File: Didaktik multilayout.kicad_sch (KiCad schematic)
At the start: 122 parts, among them J1 Conn_01x04_MountingPin, J2 AVR-ISP-6, J3 Conn_01x03, SW1 SW_Push_45deg, SW10 SW_Push_45deg, SW11 SW_Push_45deg, SW12 SW_Push_45deg, SW13 SW_Push_45deg, SW14 SW_Push_45deg, SW15 SW_Push_45deg, SW16 SW_Push_45deg, SW17 SW_Push_45deg, SW18 SW_Push_45deg, SW19 SW_Push_45deg, SW2 SW_Push_45deg, SW20 SW_Push_45deg, SW21 SW_Push_45deg, SW22 SW_Push_45deg, SW23 SW_Push_45deg, SW24 SW_Push_45deg, SW25 SW_Push_45deg, SW26 SW_Push_45deg, SW27 SW_Push_45deg, SW28 SW_Push_45deg, SW29 SW_Push_45deg, SW3 SW_Push_45deg, SW30 SW_Push_45deg, SW31 SW_Push_45deg, SW31a1 SW_Push_45deg, SW32 SW_Push_45deg, SW32a1 SW_Push_45deg, SW33 SW_Push_45deg, SW33a1 SW_Push_45deg, SW34 SW_Push_45deg, SW34a1 SW_Push_45deg, SW34b1 SW_Push_45deg, SW35 SW_Push_45deg, SW35a1 SW_Push_45deg, SW35b1 SW_Push_45deg, SW35c1 SW_Push_45deg, SW36 SW_Push_45deg, SW36a1 SW_Push_45deg, SW36b1 SW_Push_45deg, SW36c1 SW_Push_45deg, SW37 SW_Push_45deg, SW37a1 SW_Push_45deg, SW37b1 SW_Push_45deg, SW38 SW_Push_45deg, SW38a1 SW_Push_45deg, SW39 SW_Push_45deg, SW39a1 SW_Push_45deg, SW4 SW_Push_45deg, SW40 SW_Push_45deg, SW40a1 SW_Push_45deg, SW41 RotaryEncoder_Switch, SW42 RotaryEncoder_Switch, SW5 SW_Push_45deg, SW6 SW_Push_45deg, SW7 SW_Push_45deg, SW8 SW_Push_45deg, SW9 SW_Push_45deg, U1 ATmega32U4-M, Y1 Crystal_GND24_Small

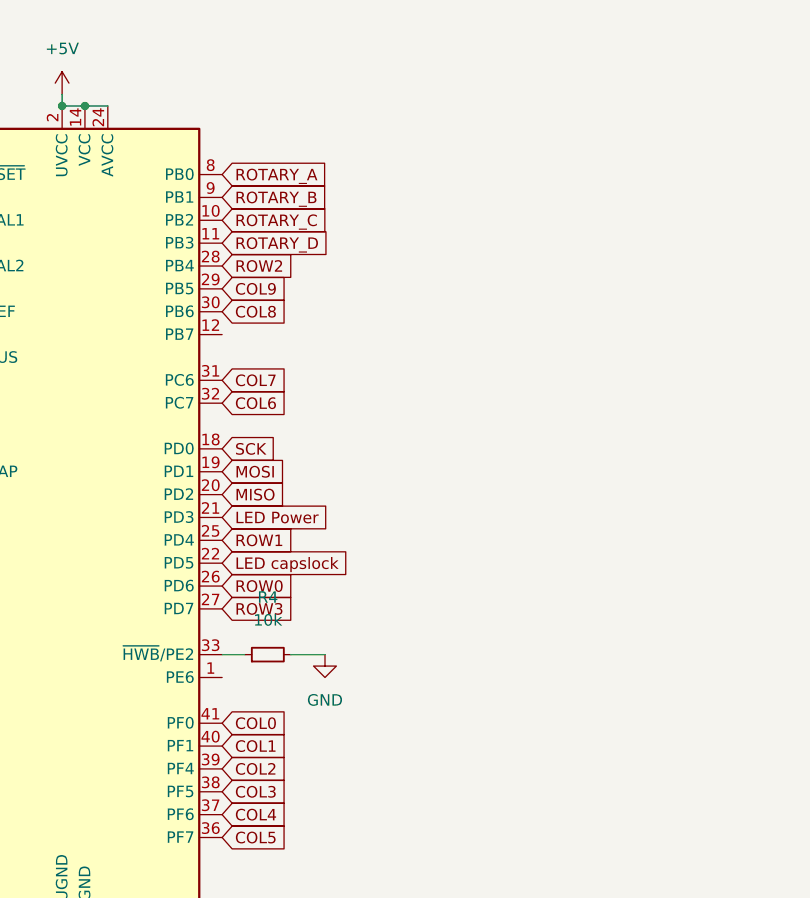
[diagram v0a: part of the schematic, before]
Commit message: added buzzer
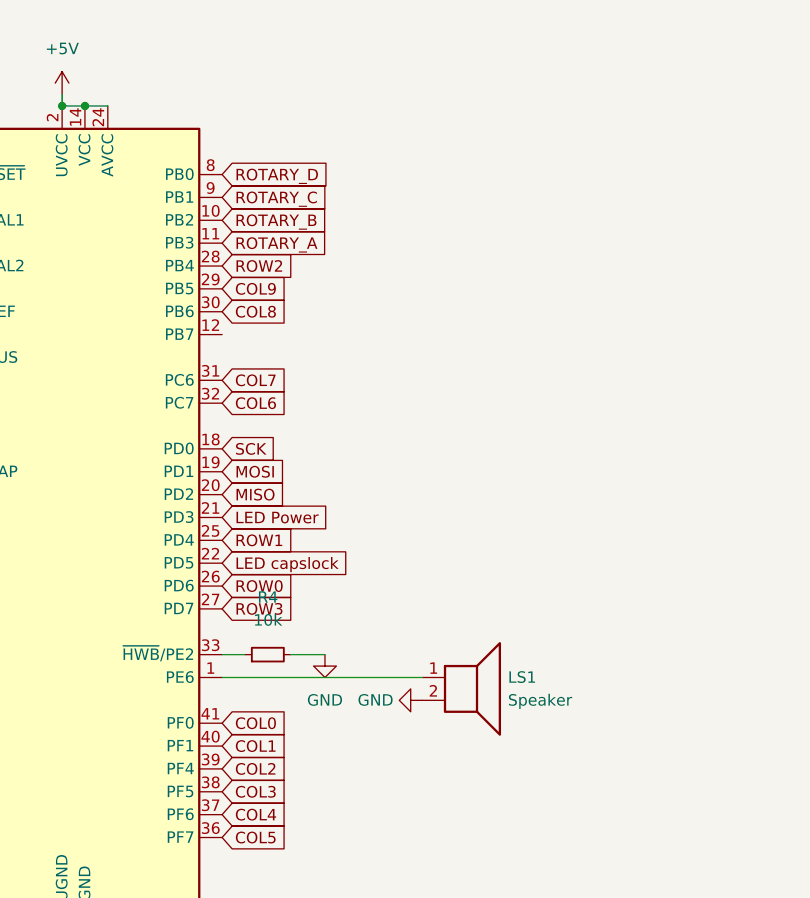
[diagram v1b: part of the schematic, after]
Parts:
- added LS1: Speaker, Keebio-Parts:AST1109MLTRQ, symbol Device:Speaker
- J3: footprint Connector_PinHeader_2.54mm:PinHeader_1x03_P2.54mm_Vertical -> Connector_PinSocket_2.00mm:PinSocket_1x03_P2.00mm_Vertical
- SW41, SW42: footprint Keebio-Parts:RotaryEncoder_Alps_EC11E-Switch_Vertical_H20mm -> Keebio-Parts:RotaryEncoder_EC11-no-legs
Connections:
- net GND: now also LS1.2
- net ROTARY_A: now also U1.11 (PB3); no longer U1.8 (PB0)
- net ROTARY_B: now also U1.10 (PB2); no longer U1.9 (PB1)
- net ROTARY_C: now also U1.9 (PB1); no longer U1.10 (PB2)
- net ROTARY_D: now also U1.8 (PB0); no longer U1.11 (PB3)
- net at U1.1 (PE6): now also LS1.1
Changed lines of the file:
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@@
     (stroke (width 0) (type default) (color 0 0 0 0))
   )
+  (wire (pts (xy 68.58 87.63) (xy 90.805 87.63))
+    (stroke (width 0) (type default) (color 0 0 0 0))
+  )
   (wire (pts (xy 196.215 88.265) (xy 196.215 107.95))
     (stroke (width 0) (type default) (color 0 0 0 0))
@@
     )
   )
-  (global_label "ROTARY_A" (shape input) (at 68.58 31.75 0) (fields_autoplaced)
+  (global_label "ROTARY_A" (shape input) (at 68.58 39.37 0) (fields_autoplaced)
     (effects (font (size 1.27 1.27)) (justify left))
-    (property "Intersheet References" "${INTERSHEET_REFS}" (id 0) (at 80.0645 31.8294 0)
+    (property "Intersheet References" "${INTERSHEET_REFS}" (id 0) (at 80.0645 39.4494 0)
       (effects (font (size 1.27 1.27)) (justify left) hide)
     )
@@
     )
   )
-  (global_label "ROTARY_B" (shape input) (at 68.58 34.29 0) (fields_autoplaced)
+  (global_label "ROTARY_B" (shape input) (at 68.58 36.83 0) (fields_autoplaced)
     (effects (font (size 1.27 1.27)) (justify left))
-    (property "Intersheet References" "${INTERSHEET_REFS}" (id 0) (at 80.246 34.3694 0)
+    (property "Intersheet References" "${INTERSHEET_REFS}" (id 0) (at 80.246 36.9094 0)
       (effects (font (size 1.27 1.27)) (justify left) hide)
     )
@@
     )
   )
-  (global_label "ROTARY_C" (shape input) (at 68.58 36.83 0) (fields_autoplaced)
+  (global_label "ROTARY_C" (shape input) (at 68.58 34.29 0) (fields_autoplaced)
     (effects (font (size 1.27 1.27)) (justify left))
-    (property "Intersheet References" "${INTERSHEET_REFS}" (id 0) (at 80.246 36.7506 0)
+    (property "Intersheet References" "${INTERSHEET_REFS}" (id 0) (at 80.246 34.2106 0)
       (effects (font (size 1.27 1.27)) (justify left) hide)
     )
@@
     )
   )
-  (global_label "ROTARY_D" (shape input) (at 68.58 39.37 0) (fields_autoplaced)
+  (global_label "ROTARY_D" (shape input) (at 68.58 31.75 0) (fields_autoplaced)
     (effects (font (size 1.27 1.27)) (justify left))
-    (property "Intersheet References" "${INTERSHEET_REFS}" (id 0) (at 80.246 39.2906 0)
+    (property "Intersheet References" "${INTERSHEET_REFS}" (id 0) (at 80.246 31.6706 0)
       (effects (font (size 1.27 1.27)) (justify left) hide)
     )
@@
     (pin "2")
   )
+  (symbol (lib_id "power:GND") (at 90.805 90.17 270) (unit 1)
+    (in_bom yes) (on_board yes) (fields_autoplaced)
+    (property "Reference" "#PWR0125" (id 0) (at 84.455 90.17 0)
+      (effects (font (size 1.27 1.27)) hide)
+    )
+    (property "Value" "GND" (id 1) (at 87.63 90.1699 90)
+      (effects (font (size 1.27 1.27)) (justify right))
+    )
+    (property "Footprint" "" (id 2) (at 90.805 90.17 0)
+      (effects (font (size 1.27 1.27)) hide)
+    )
+    (property "Datasheet" "" (id 3) (at 90.805 90.17 0)
+      (effects (font (size 1.27 1.27)) hide)
+    )
+    (pin "1")
+  )
   (symbol (lib_id "power:GND") (at 48.26 115.57 0) (unit 1)
     (in_bom yes) (on_board yes) (fields_autoplaced)
@@
     (property "Reference" "J3" (id 0) (at 131.445 120.015 0))
     (property "Value" "Conn_01x03" (id 1) (at 131.445 130.175 0))
-    (property "Footprint" "Connector_PinHeader_2.54mm:PinHeader_1x03_P2.54mm_Vertical" (id 2) (at 131.445 125.095 0)
+    (property "Footprint" "Connector_PinSocket_2.00mm:PinSocket_1x03_P2.00mm_Vertical" (id 2) (at 131.445 125.095 0)
       (effects (font (size 1.27 1.27)) hide)
     )
@@
     (property "Reference" "SW42" (id 0) (at 239.395 82.55 0))
     (property "Value" "RotaryEncoder_Switch" (id 1) (at 239.395 80.01 0))
-    (property "Footprint" "Keebio-Parts:RotaryEncoder_Alps_EC11E-Switch_Vertical_H20mm" (id 2) (at 243.205 76.454 0)
+    (property "Footprint" "Keebio-Parts:RotaryEncoder_EC11-no-legs" (id 2) (at 243.205 76.454 0)
       (effects (font (size 1.27 1.27)) hide)
     )
@@
     (property "Reference" "SW41" (id 0) (at 153.67 28.575 0))
     (property "Value" "RotaryEncoder_Switch" (id 1) (at 153.67 31.115 0))
-    (property "Footprint" "Keebio-Parts:RotaryEncoder_Alps_EC11E-Switch_Vertical_H20mm" (id 2) (at 149.86 34.671 0)
+    (property "Footprint" "Keebio-Parts:RotaryEncoder_EC11-no-legs" (id 2) (at 149.86 34.671 0)
       (effects (font (size 1.27 1.27)) hide)
     )
@@
     (pin "2")
   )
+  (symbol (lib_id "Device:Speaker") (at 95.885 87.63 0) (unit 1)
+    (in_bom yes) (on_board yes) (fields_autoplaced)
+    (property "Reference" "LS1" (id 0) (at 100.33 87.6299 0)
+      (effects (font (size 1.27 1.27)) (justify left))
+    )
+    (property "Value" "Speaker" (id 1) (at 100.33 90.1699 0)
+      (effects (font (size 1.27 1.27)) (justify left))
+    )
+    (property "Footprint" "Keebio-Parts:AST1109MLTRQ" (id 2) (at 95.885 92.71 0)
+      (effects (font (size 1.27 1.27)) hide)
+    )
+    (property "Datasheet" "~" (id 3) (at 95.631 88.9 0)
+      (effects (font (size 1.27 1.27)) hide)
+    )
+    (pin "1")
+    (pin "2")
+  )
   (symbol (lib_id "Switch:SW_Push_45deg") (at 199.39 105.41 0) (mirror y) (unit 1)
     (in_bom yes) (on_board yes)
@@
       (reference "#PWR0124") (unit 1) (value "GND") (footprint "")
     )
+    (path "/46e8824a-8f30-44a6-8611-6e7599dbffe8"
+      (reference "#PWR0125") (unit 1) (value "GND") (footprint "")
+    )
     (path "/4288a19a-13d9-4091-890e-2cc91277147e"
       (reference "C1") (unit 1) (value "0.1uF") (footprint "Capacitor_SMD:C_0402_1005Metric")
@@
     )
     (path "/909e0f83-af71-499c-861a-44ecae1cdab9"
-      (reference "J3") (unit 1) (value "Conn_01x03") (footprint "Connector_PinHeader_2.54mm:PinHeader_1x03_P2.54mm_Vertical")
+      (reference "J3") (unit 1) (value "Conn_01x03") (footprint "Connector_PinSocket_2.00mm:PinSocket_1x03_P2.00mm_Vertical")
+    )
+    (path "/fbecd2a9-a948-4ba1-8e78-655fa59a6c74"
+      (reference "LS1") (unit 1) (value "Speaker") (footprint "Keebio-Parts:AST1109MLTRQ")
     )
     (path "/1b233532-9656-4e4e-a0b7-8260db2f2d5f"
@@
     )
     (path "/b5d6c90d-09f6-4204-96c6-5159b8bf8ade"
-      (reference "SW41") (unit 1) (value "RotaryEncoder_Switch") (footprint "Keebio-Parts:RotaryEncoder_Alps_EC11E-Switch_Vertical_H20mm")
+      (reference "SW41") (unit 1) (value "RotaryEncoder_Switch") (footprint "Keebio-Parts:RotaryEncoder_EC11-no-legs")
     )
     (path "/b188310f-7fb9-45a6-a509-13d28fe15160"
-      (reference "SW42") (unit 1) (value "RotaryEncoder_Switch") (footprint "Keebio-Parts:RotaryEncoder_Alps_EC11E-Switch_Vertical_H20mm")
+      (reference "SW42") (unit 1) (value "RotaryEncoder_Switch") (footprint "Keebio-Parts:RotaryEncoder_EC11-no-legs")
     )
     (path "/24a36d74-2c9b-468a-8a3d-4eb2fe2b6c67"

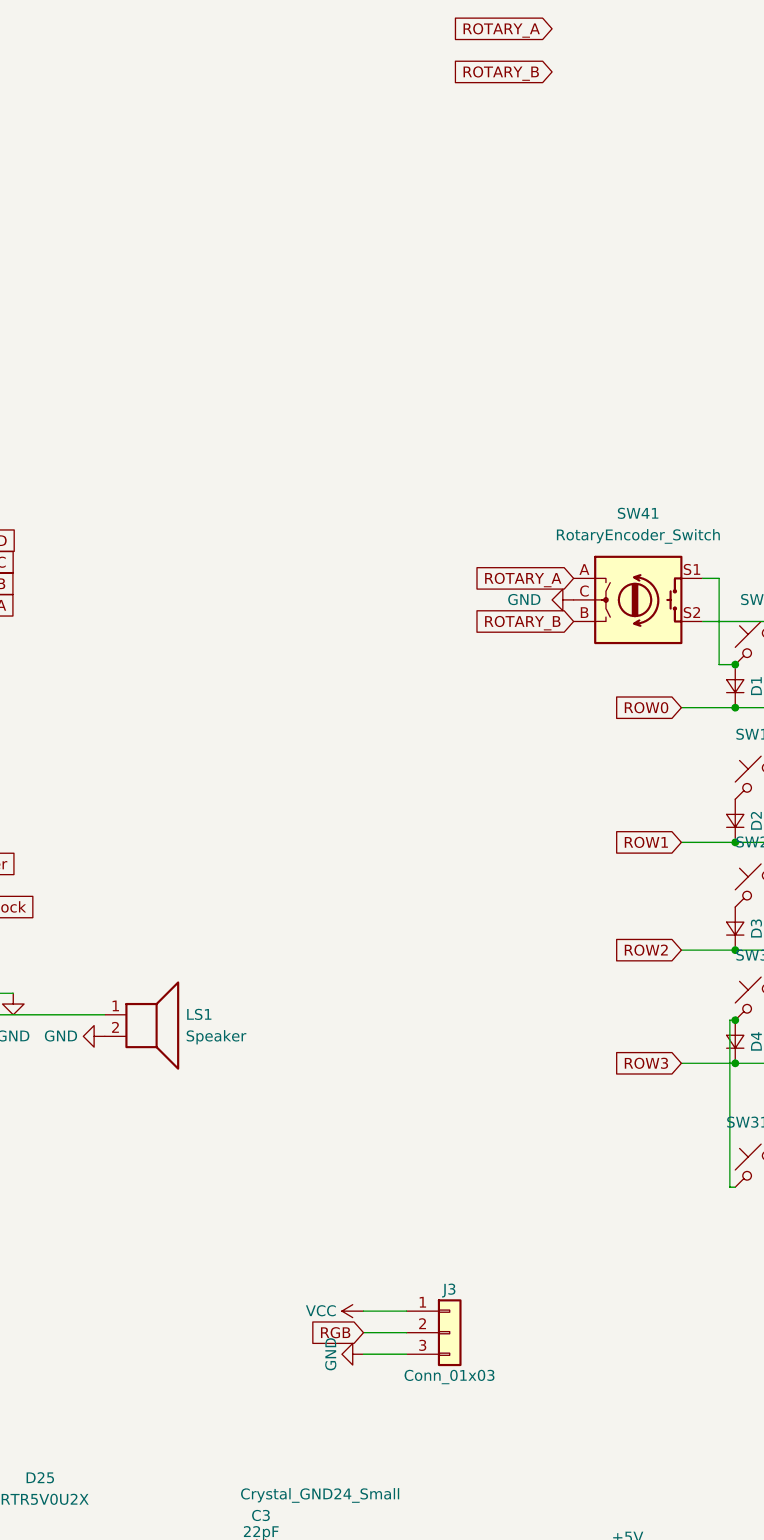
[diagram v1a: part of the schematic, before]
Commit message: created production files, pdfs for review
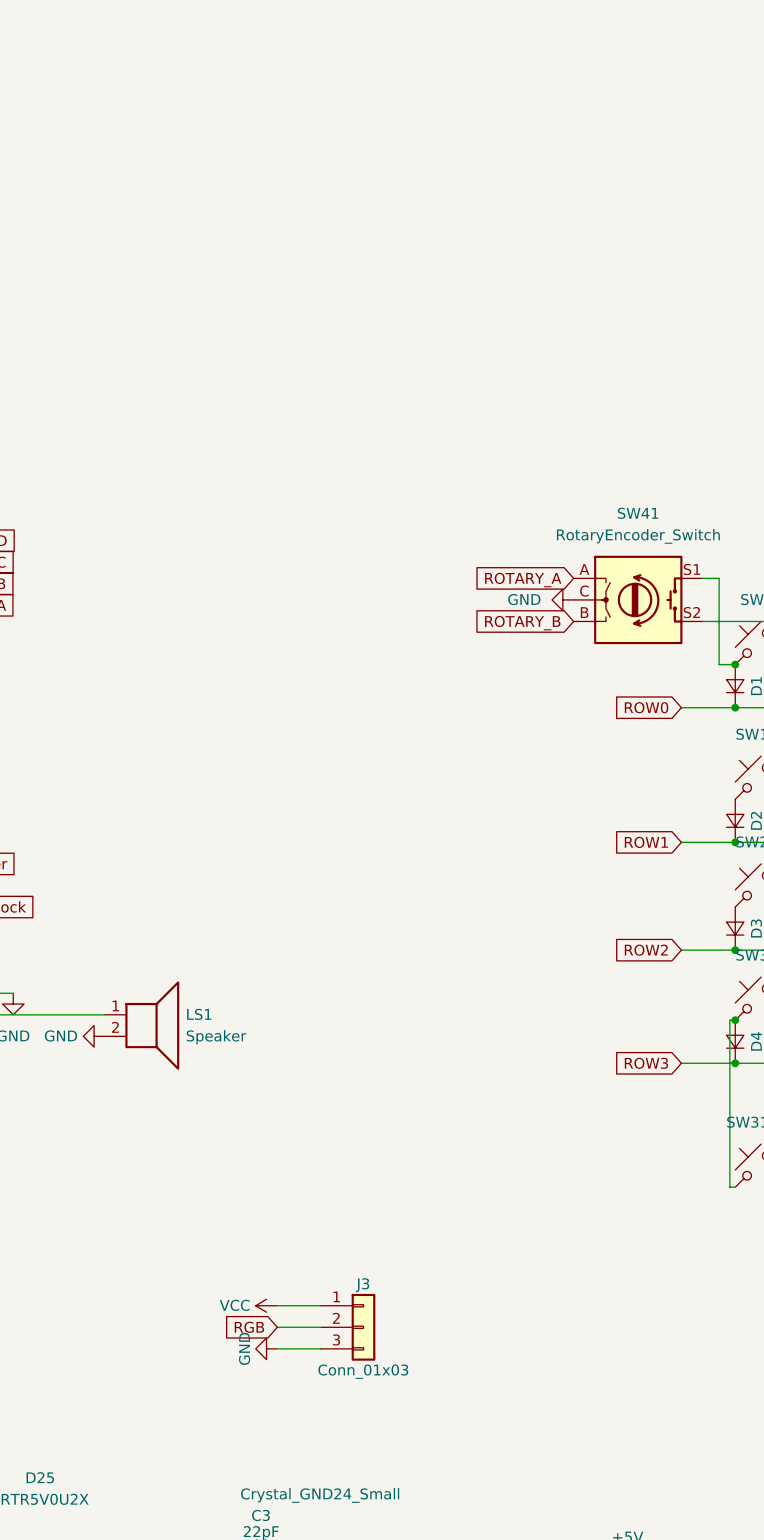
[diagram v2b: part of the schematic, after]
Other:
- moved on the sheet: J3
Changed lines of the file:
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@@
     (stroke (width 0) (type default) (color 0 0 0 0))
   )
-  (wire (pts (xy 121.285 122.555) (xy 126.365 122.555))
+  (wire (pts (xy 111.125 121.92) (xy 116.205 121.92))
     (stroke (width 0) (type default) (color 0 0 0 0))
   )
@@
     (stroke (width 0) (type default) (color 0 0 0 0))
   )
-  (wire (pts (xy 121.285 127.635) (xy 126.365 127.635))
+  (wire (pts (xy 111.125 127) (xy 116.205 127))
     (stroke (width 0) (type default) (color 0 0 0 0))
   )
@@
     (stroke (width 0) (type default) (color 0 0 0 0))
   )
-  (wire (pts (xy 121.285 125.095) (xy 126.365 125.095))
+  (wire (pts (xy 111.125 124.46) (xy 116.205 124.46))
     (stroke (width 0) (type default) (color 0 0 0 0))
   )
@@
     )
   )
-  (global_label "ROTARY_B" (shape input) (at 143.51 -23.495 180) (fields_autoplaced)
-    (effects (font (size 1.27 1.27)) (justify right))
-    (property "Intersheet References" "${INTERSHEET_REFS}" (id 0) (at 131.844 -23.5744 0)
-      (effects (font (size 1.27 1.27)) (justify right) hide)
-    )
-  )
   (global_label "ROTARY_A" (shape input) (at 146.05 36.195 180) (fields_autoplaced)
     (effects (font (size 1.27 1.27)) (justify right))
@@
     )
   )
-  (global_label "ROTARY_A" (shape input) (at 143.51 -28.575 180) (fields_autoplaced)
-    (effects (font (size 1.27 1.27)) (justify right))
-    (property "Intersheet References" "${INTERSHEET_REFS}" (id 0) (at 132.0255 -28.6544 0)
-      (effects (font (size 1.27 1.27)) (justify right) hide)
-    )
-  )
   (global_label "COL9" (shape input) (at 68.58 44.45 0) (fields_autoplaced)
     (effects (font (size 1.27 1.27)) (justify left))
@@
     )
   )
-  (global_label "RGB" (shape input) (at 121.285 125.095 180) (fields_autoplaced)
+  (global_label "RGB" (shape input) (at 111.125 124.46 180) (fields_autoplaced)
     (effects (font (size 1.27 1.27)) (justify right))
-    (property "Intersheet References" "${INTERSHEET_REFS}" (id 0) (at -40.005 77.47 0)
+    (property "Intersheet References" "${INTERSHEET_REFS}" (id 0) (at -50.165 76.835 0)
       (effects (font (size 1.27 1.27)) hide)
     )
@@
     (pin "2")
   )
-  (symbol (lib_id "power:VCC") (at 121.285 122.555 90) (unit 1)
-    (in_bom yes) (on_board yes) (fields_autoplaced)
-    (property "Reference" "#PWR0115" (id 0) (at 125.095 122.555 0)
-      (effects (font (size 1.27 1.27)) hide)
-    )
-    (property "Value" "VCC" (id 1) (at 118.11 122.5549 90)
+  (symbol (lib_id "power:VCC") (at 111.125 121.92 90) (unit 1)
+    (in_bom yes) (on_board yes) (fields_autoplaced)
+    (property "Reference" "#PWR0115" (id 0) (at 114.935 121.92 0)
+      (effects (font (size 1.27 1.27)) hide)
+    )
+    (property "Value" "VCC" (id 1) (at 107.95 121.9199 90)
       (effects (font (size 1.27 1.27)) (justify left))
     )
-    (property "Footprint" "" (id 2) (at 121.285 122.555 0)
-      (effects (font (size 1.27 1.27)) hide)
-    )
-    (property "Datasheet" "" (id 3) (at 121.285 122.555 0)
+    (property "Footprint" "" (id 2) (at 111.125 121.92 0)
+      (effects (font (size 1.27 1.27)) hide)
+    )
+    (property "Datasheet" "" (id 3) (at 111.125 121.92 0)
       (effects (font (size 1.27 1.27)) hide)
     )
@@
     (pin "2")
   )
-  (symbol (lib_id "alpha_pro_micro-rescue:Conn_01x03") (at 131.445 125.095 0) (unit 1)
-    (in_bom yes) (on_board yes)
-    (property "Reference" "J3" (id 0) (at 131.445 120.015 0))
-    (property "Value" "Conn_01x03" (id 1) (at 131.445 130.175 0))
-    (property "Footprint" "Connector_PinSocket_2.00mm:PinSocket_1x03_P2.00mm_Vertical" (id 2) (at 131.445 125.095 0)
-      (effects (font (size 1.27 1.27)) hide)
-    )
-    (property "Datasheet" "" (id 3) (at 131.445 125.095 0)
+  (symbol (lib_id "alpha_pro_micro-rescue:Conn_01x03") (at 121.285 124.46 0) (unit 1)
+    (in_bom yes) (on_board yes)
+    (property "Reference" "J3" (id 0) (at 121.285 119.38 0))
+    (property "Value" "Conn_01x03" (id 1) (at 121.285 129.54 0))
+    (property "Footprint" "Connector_PinSocket_2.00mm:PinSocket_1x03_P2.00mm_Vertical" (id 2) (at 121.285 124.46 0)
+      (effects (font (size 1.27 1.27)) hide)
+    )
+    (property "Datasheet" "" (id 3) (at 121.285 124.46 0)
       (effects (font (size 1.27 1.27)) hide)
     )
@@
     (pin "1")
   )
-  (symbol (lib_id "power:GND") (at 121.285 127.635 270) (unit 1)
-    (in_bom yes) (on_board yes)
-    (property "Reference" "#PWR0120" (id 0) (at 114.935 127.635 0)
-      (effects (font (size 1.27 1.27)) hide)
-    )
-    (property "Value" "GND" (id 1) (at 117.475 127.635 0))
-    (property "Footprint" "" (id 2) (at 121.285 127.635 0)
-      (effects (font (size 1.27 1.27)) hide)
-    )
-    (property "Datasheet" "" (id 3) (at 121.285 127.635 0)
-      (effects (font (size 1.27 1.27)) hide)
-    )
+  (symbol (lib_id "power:GND") (at 111.125 127 270) (unit 1)
+    (in_bom yes) (on_board yes)
+    (property "Reference" "#PWR0120" (id 0) (at 104.775 127 0)
+      (effects (font (size 1.27 1.27)) hide)
+    )
+    (property "Value" "GND" (id 1) (at 107.315 127 0))
+    (property "Footprint" "" (id 2) (at 111.125 127 0)
+      (effects (font (size 1.27 1.27)) hide)
+    )
+    (property "Datasheet" "" (id 3) (at 111.125 127 0)
+      (effects (font (size 1.27 1.27)) hide)
+    )
